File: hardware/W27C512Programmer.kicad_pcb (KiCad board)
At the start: 2 copper layers, 68.6 x 53.3 mm, 26 parts, among them Q1 Q_NPN_BCE, U1 AP3012, U2 LM339, U3 74HC595, U4 74HC595, U5 w27C512

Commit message: Getting ready for PCB..
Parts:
- added C10: 200uF, Capacitor_SMD:CP_Elec_6.3x5.4, F.Cu at (118.1, 36.8)
- added C11: 10uF, Capacitor_SMD:CP_Elec_5x5.4, F.Cu at (127.3, 54.6)
- added C7: 100nF, Capacitor_SMD:C_0603_1608Metric, F.Cu at (121.3, 90.2)
- added C8: 100nF, Capacitor_SMD:C_0603_1608Metric, F.Cu at (92.9, 55.6)
- added C9: 10uF, Capacitor_SMD:C_1206_3216Metric, F.Cu at (144.6, 57.1)
- added D10: 1N5819, Diode_SMD:D_SOD-123, F.Cu at (106.7, 55.2)
- added D11: 1N5819, Diode_SMD:D_SOD-123, F.Cu at (156.3, 71.8)
- added D12: 1N5819, Diode_SMD:D_SOD-123, F.Cu at (113.0, 55.2)
- added D2: GREEN, LED_SMD:LED_0603_1608Metric, F.Cu at (143.0, 95.2)
- added D3: GREEN, LED_SMD:LED_0603_1608Metric, F.Cu at (144.7, 95.2)
- added D4: GREEN, LED_SMD:LED_0603_1608Metric, F.Cu at (146.3, 95.2)
- added D5: GREEN, LED_SMD:LED_0603_1608Metric, F.Cu at (148.0, 95.2)
- added D6: GREEN, LED_SMD:LED_0603_1608Metric, F.Cu at (149.6, 95.2)
- added D7: GREEN, LED_SMD:LED_0603_1608Metric, F.Cu at (151.3, 95.2)
- added D8: GREEN, LED_SMD:LED_0603_1608Metric, F.Cu at (153.0, 95.2)
- added D9: RED, LED_SMD:LED_0603_1608Metric, F.Cu at (154.7, 95.2)
- added J1: CTRL, Connector_PinHeader_2.54mm:PinHeader_1x08_P2.54mm_Vertical, F.Cu at (134.6, 86.4)
- added J2: MSB, Connector_PinHeader_2.54mm:PinHeader_1x08_P2.54mm_Vertical, F.Cu at (114.3, 86.4)
- added J3: LSB, Connector_PinHeader_2.54mm:PinHeader_1x08_P2.54mm_Vertical, F.Cu at (94.0, 86.4)
- added J4: Ext_UART, Connector_PinHeader_2.54mm:PinHeader_1x03_P2.54mm_Vertical, F.Cu at (176.9, 52.1)
- added JP1: 24pin ROM VCC, Connector_PinHeader_2.54mm:PinHeader_1x03_P2.54mm_Vertical, F.Cu at (96.5, 56.5)
- added JP2: >=SST39SF020 needs A17, Connector_PinHeader_2.54mm:PinHeader_1x03_P2.54mm_Vertical, F.Cu at (96.6, 52.8)
- added Q2: 2N3906, Package_TO_SOT_SMD:SOT-23, F.Cu at (155.1, 54.1)
- added Q3: 2N3904, Package_TO_SOT_SMD:SOT-23, F.Cu at (155.0, 64.8)
- added Q4: 2N3904, Package_TO_SOT_SMD:SOT-23, F.Cu at (154.9, 84.0)
- added Q5: 2N3904, Package_TO_SOT_SMD:SOT-23, F.Cu at (153.0, 74.6)
- added Q6: 2N3906, Package_TO_SOT_SMD:SOT-23, F.Cu at (155.0, 61.2)
- added Q7: 2N3906, Package_TO_SOT_SMD:SOT-23, F.Cu at (154.9, 80.5)
- added Q8: 2N3906, Package_TO_SOT_SMD:SOT-23, F.Cu at (153.0, 71.0)
- added R12: 4k7, Resistor_SMD:R_0603_1608Metric, F.Cu at (144.7, 92.0)
- added R13: 4k7, Resistor_SMD:R_0603_1608Metric, F.Cu at (146.3, 92.0)
- added R14: 4k7, Resistor_SMD:R_0603_1608Metric, F.Cu at (148.0, 92.0)
- added R15: 4k7, Resistor_SMD:R_0603_1608Metric, F.Cu at (149.6, 92.0)
- added R16: 4k7, Resistor_SMD:R_0603_1608Metric, F.Cu at (151.3, 92.0)
- added R17: 4k7, Resistor_SMD:R_0603_1608Metric, F.Cu at (153.0, 92.0)
- added R18: 4k7, Resistor_SMD:R_0603_1608Metric, F.Cu at (154.7, 92.0)
- added R19: 22k, Resistor_SMD:R_0603_1608Metric, F.Cu at (108.9, 55.3)
- added R20: 22k, Resistor_SMD:R_0603_1608Metric, F.Cu at (106.9, 83.2)
- added R21: 22k, Resistor_SMD:R_0603_1608Metric, F.Cu at (110.5, 55.2)
- added R22: 1k, Resistor_SMD:R_0603_1608Metric, F.Cu at (172.7, 52.1)
- added R23: 22k, Resistor_SMD:R_0603_1608Metric, F.Cu at (152.2, 64.9)
- added R24: 22k, Resistor_SMD:R_0603_1608Metric, F.Cu at (151.5, 83.9)
- added R25: 22k, Resistor_SMD:R_0603_1608Metric, F.Cu at (149.3, 73.6)
- added R26: 4k7, Resistor_SMD:R_0603_1608Metric, F.Cu at (150.6, 61.3)
- added R27: 4k7, Resistor_SMD:R_0603_1608Metric, F.Cu at (149.8, 80.6)
- added R28: 4k7, Resistor_SMD:R_0603_1608Metric, F.Cu at (149.3, 71.9)
- added R29: 22k, Resistor_SMD:R_0603_1608Metric, F.Cu at (152.2, 61.3)
- added R30: 22k, Resistor_SMD:R_0603_1608Metric, F.Cu at (151.6, 80.5)
- added R31: 22k, Resistor_SMD:R_0603_1608Metric, F.Cu at (149.3, 70.2)
- added RV1: 50k, Potentiometer_SMD:Potentiometer_Bourns_TC33X_Vertical, F.Cu at (134.4, 56.5)
- C1: value 1uF -> 10uF; footprint Capacitor_SMD:C_0805_2012Metric -> Capacitor_SMD:C_1206_3216Metric
- C2, C4, C5, C6: footprint Capacitor_SMD:C_0805_2012Metric -> Capacitor_SMD:C_0603_1608Metric
- C3: value 1uF -> 100nF; footprint Capacitor_SMD:C_0805_2012Metric -> Capacitor_SMD:C_0603_1608Metric
- Q1: value Q_NPN_BCE -> 2N3904
- R1: value 9.8k -> 22k; footprint Resistor_SMD:R_0805_2012Metric -> Resistor_SMD:R_0603_1608Metric
- R10, R3, R6, R9: value 9.8k -> 4k7; footprint Resistor_SMD:R_0805_2012Metric -> Resistor_SMD:R_0603_1608Metric
- R11: value 470 -> 4k7; footprint Resistor_SMD:R_0805_2012Metric -> Resistor_SMD:R_0603_1608Metric
- R2: value 100k -> 22k; footprint Resistor_SMD:R_0805_2012Metric -> Resistor_SMD:R_0603_1608Metric
- R4: value 56k -> 22k; footprint Resistor_SMD:R_0805_2012Metric -> Resistor_SMD:R_0603_1608Metric
- R5: value 22k -> 270k; footprint Resistor_SMD:R_0805_2012Metric -> Resistor_SMD:R_0603_1608Metric
- R7: value 68k -> 4k7; footprint Resistor_SMD:R_0805_2012Metric -> Resistor_SMD:R_0603_1608Metric
- R8: value 1k5 -> 22k; footprint Resistor_SMD:R_0805_2012Metric -> Resistor_SMD:R_0603_1608Metric
- U1: value AP3012 -> MIC2288
- U2: value LM339 -> 74HC573; footprint Package_SO:SOIC-14_3.9x8.7mm_P1.27mm -> Package_SO:TSSOP-20_4.4x6.5mm_P0.65mm
- U3, U4: value 74HC595 -> 74HC573; footprint Package_SO:SOIC-16_3.9x9.9mm_P1.27mm -> Package_SO:TSSOP-20_4.4x6.5mm_P0.65mm
- U5: value w27C512 -> 28/32 pin ROM; footprint Socket:DIP_Socket-28_W11.9_W12.7_W15.24_W17.78_W18.5_3M_228-1277-00-0602J -> Socket:DIP_Socket-32_W11.9_W12.7_W15.24_W17.78_W18.5_3M_232-1285-00-0602J
- moved C3 61.4 mm to (91.1, 55.7), turned to 90 degrees
- moved C2 53.7 mm to (91.0, 52.4), turned to -90 degrees
- moved C6 47.8 mm to (97.2, 90.2), turned to -90 degrees
- moved U2 42.4 mm to (102.9, 92.7)
- moved R4 41.3 mm to (150.5, 54.1), turned to -90 degrees
- moved R5 39.7 mm to (150.5, 57.6), turned to -90 degrees
- moved R9 39.3 mm to (140.3, 55.9)
- moved R8 34.3 mm to (129.3, 59.7), turned to 180 degrees
- moved R6 33.0 mm to (140.3, 54.3)
- moved R7 31.6 mm to (140.3, 57.8)
- moved R10 29.9 mm to (140.3, 52.7), turned to 180 degrees
- moved R1 25.5 mm to (147.3, 53.3), turned to -90 degrees
- moved C1 21.0 mm to (144.6, 48.3), turned to 180 degrees
- moved D1 17.4 mm to (139.3, 48.3)
- moved L1 16.5 mm to (144.4, 50.8), turned to 180 degrees
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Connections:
- A1 pad 15: Net-(A1-Pad15) -> D0
- A1 pad 16: Net-(A1-Pad16) -> D1
- A1 pad 17: Net-(A1-Pad17) -> D2
- A1 pad 18: Net-(A1-Pad18) -> D3
- A1 pad 19: Net-(A1-Pad19) -> D4
- A1 pad 20: Net-(A1-Pad20) -> D5
- A1 pad 21: Net-(A1-Pad21) -> D6
- A1 pad 22: Net-(A1-Pad22) -> D7
- A1 pad 23: SRClock -> RLSBLE
- A1 pad 24: SRData -> RMSBLE
- A1 pad 25: ~{ROM_CE} -> ~{ROM_OE}
- A1 pad 26: VPE_ENABLE -> CTRL_LE
- A1 pad 27: ~{VPE_TO_VPP} -> unconnected-(A1-Pad27)
- A1 pad 28: unconnected-(A1-Pad28) -> ~{ROM_CE}
- A1 pad 9: ~{VPE_DISABLE} -> unconnected-(A1-Pad9)
- C3 pad 1: VPE -> +5V
- C6 pad 1: Net-(C6-Pad1) -> +5V
- Q1 pad 1: Net-(Q1-Pad1) -> GND
- Q1 pad 2: VPE -> Net-(Q1-Pad2)
- R1 pad 2: ~{VPE_DISABLE} -> ~{REG_DISABLE}
- R10 pad 1: VPE -> Net-(R10-Pad1)
- R10 pad 2: Net-(R10-Pad2) -> GND
- R11 pad 1: Net-(Q1-Pad3) -> Net-(D2-Pad1)
- R2 pad 1: VPE -> A16
- R2 pad 2: Net-(R2-Pad2) -> Net-(Q1-Pad2)
- R3 pad 1: Net-(R2-Pad2) -> Net-(Q1-Pad3)
- R3 pad 2: GND -> Net-(Q2-Pad2)
- R4 pad 1: +5V -> VPE
- R4 pad 2: Net-(C6-Pad1) -> Net-(Q2-Pad2)
- R5 pad 1: Net-(C6-Pad1) -> Net-(Q2-Pad3)
- R5 pad 2: GND -> Net-(R10-Pad1)
- R6 pad 1: VPE -> Net-(R6-Pad1)
- R6 pad 2: Net-(R6-Pad2) -> Net-(R10-Pad1)
- R7 pad 1: Net-(R6-Pad2) -> Net-(R6-Pad1)
- R7 pad 2: Net-(R7-Pad2) -> Net-(R10-Pad1)
- R8 pad 1: Net-(R8-Pad1) -> VPE
- R8 pad 2: Net-(R10-Pad2) -> Net-(R8-Pad2)
- R9 pad 1: Net-(Q1-Pad1) -> Net-(R6-Pad1)
- R9 pad 2: Net-(R6-Pad2) -> Net-(R10-Pad1)
- U1 pad 3: Net-(R2-Pad2) -> Net-(R10-Pad1)
- U1 pad 4: ~{VPE_DISABLE} -> ~{REG_DISABLE}
- U2 pad 1: Net-(R7-Pad2) -> GND
- U2 pad 10: Net-(C6-Pad1) -> GND
- U2 pad 11: VPE_ENABLE -> RLSBLE
- U2 pad 12: GND -> Net-(J3-Pad8)
- U2 pad 13: Net-(R10-Pad2) -> Net-(J3-Pad7)
- U2 pad 14: unconnected-(U2-Pad14) -> Net-(J3-Pad6)
- U2 pad 2: Net-(R6-Pad2) -> D0
- U2 pad 3: VPE -> D1
- U2 pad 4: Net-(C6-Pad1) -> D2
- U2 pad 5: VPE_ENABLE -> D3
- U2 pad 6: Net-(C6-Pad1) -> D4
- U2 pad 7: ~{VPE_TO_VPP} -> D5
- U2 pad 8: Net-(C6-Pad1) -> D6
- U2 pad 9: unconnected-(U2-Pad9) -> D7
- U3 pad 1: Net-(U3-Pad1) -> GND
- U3 pad 10: Net-(U3-Pad10) -> GND
- U3 pad 11: SRClock -> RMSBLE
- U3 pad 12: SRClock -> Net-(D11-Pad2)
- U3 pad 13: GND -> Net-(J2-Pad7)
- U3 pad 14: SRData -> Net-(J2-Pad6)
- U3 pad 15: Net-(U3-Pad15) -> Net-(J2-Pad5)
- U3 pad 16: +5V -> Net-(J2-Pad4)
- U3 pad 2: Net-(U3-Pad2) -> D0
- U3 pad 3: Net-(U3-Pad3) -> D1
- U3 pad 4: Net-(U3-Pad4) -> D2
- U3 pad 5: Net-(U3-Pad5) -> D3
- U3 pad 6: Net-(U3-Pad6) -> D4
- U3 pad 7: Net-(U3-Pad7) -> D5
- U3 pad 8: GND -> D6
- U3 pad 9: Net-(U3-Pad9) -> D7
- U4 pad 1: Net-(R8-Pad1) -> GND
- U4 pad 10: Net-(U3-Pad10) -> GND
- U4 pad 11: SRClock -> CTRL_LE
- U4 pad 12: SRClock -> ~{REG_DISABLE}
- U4 pad 13: GND -> ~{RW}
- U4 pad 14: Net-(U3-Pad9) -> A18
- U4 pad 15: Net-(U4-Pad15) -> A17
- U4 pad 16: +5V -> P1_VPP_ENABLE
- U4 pad 2: Net-(U4-Pad2) -> D0
- U4 pad 3: Net-(U4-Pad3) -> D1
- U4 pad 4: Net-(U4-Pad4) -> D2
- U4 pad 5: Net-(U4-Pad5) -> D3
- U4 pad 6: Net-(U4-Pad6) -> D4
- U4 pad 7: Net-(U4-Pad7) -> D5
- U4 pad 8: GND -> D6
- U4 pad 9: unconnected-(U4-Pad9) -> D7
- U5 pad 1: Net-(U4-Pad7) -> A18
- U5 pad 10: Net-(U3-Pad15) -> Net-(J3-Pad3)
- U5 pad 11: Net-(A1-Pad15) -> Net-(J3-Pad2)
- U5 pad 12: Net-(A1-Pad16) -> Net-(J3-Pad1)
- U5 pad 13: Net-(A1-Pad17) -> D0
- U5 pad 14: GND -> D1
- U5 pad 15: Net-(A1-Pad18) -> D2
- U5 pad 16: Net-(A1-Pad19) -> GND
- U5 pad 17: Net-(A1-Pad20) -> D3
- U5 pad 18: Net-(A1-Pad21) -> D4
- U5 pad 19: Net-(A1-Pad22) -> D5
- U5 pad 2: Net-(U4-Pad4) -> A16
- U5 pad 20: ~{ROM_CE} -> D6
- U5 pad 21: Net-(U4-Pad2) -> D7
- U5 pad 22: Net-(Q1-Pad3) -> ~{ROM_CE}
- U5 pad 23: Net-(U4-Pad3) -> Net-(J2-Pad3)
- U5 pad 24: Net-(R10-Pad2) -> Net-(D12-Pad1)
- U5 pad 25: Net-(U4-Pad15) -> Net-(J2-Pad4)
- U5 pad 26: Net-(U4-Pad5) -> Net-(D10-Pad1)
- U5 pad 27: Net-(U4-Pad6) -> Net-(J2-Pad1)
- U5 pad 28: +5V -> Net-(JP1-Pad2)
- U5 pad 3: Net-(U3-Pad7) -> Net-(D11-Pad1)
- U5 pad 4: Net-(U3-Pad6) -> Net-(J2-Pad5)
- U5 pad 5: Net-(U3-Pad5) -> Net-(J3-Pad8)
- U5 pad 6: Net-(U3-Pad4) -> Net-(J3-Pad7)
- U5 pad 7: Net-(U3-Pad3) -> Net-(J3-Pad6)
- U5 pad 8: Net-(U3-Pad2) -> Net-(J3-Pad5)
- U5 pad 9: Net-(U3-Pad1) -> Net-(J3-Pad4)
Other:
- board text added: "Reg. ON"

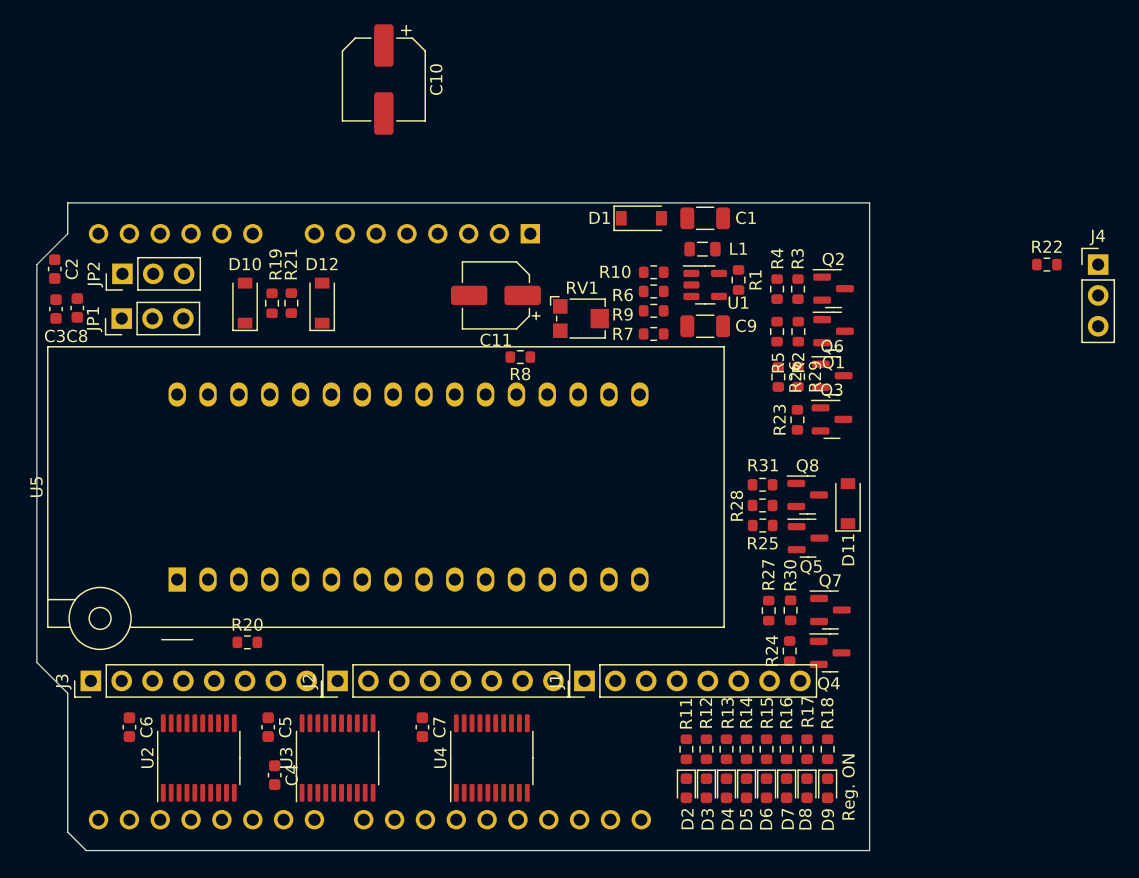
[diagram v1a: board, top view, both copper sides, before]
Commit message: PCB probably somewhat complete
Completely untested PCB. Maybe it works. Maybe I should look for someone to review...
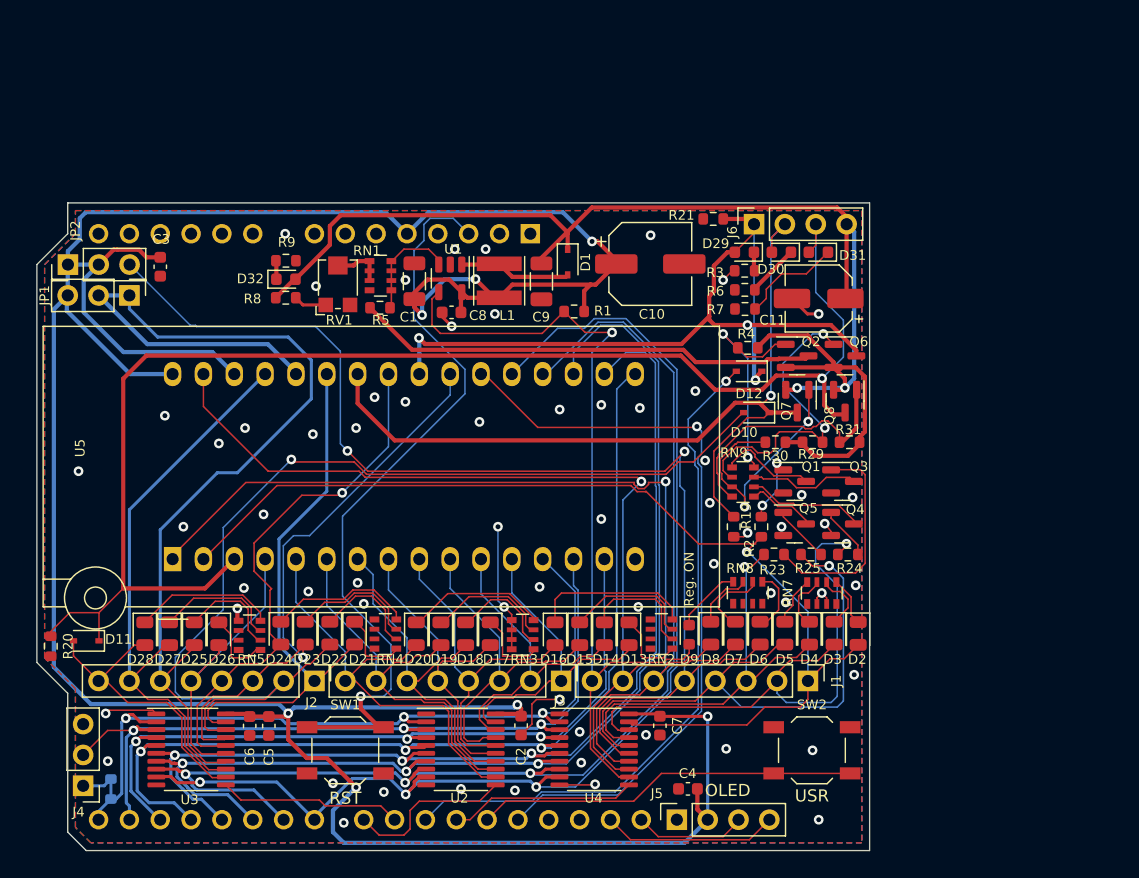
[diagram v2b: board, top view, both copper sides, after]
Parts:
- removed R10, R11, R12, R13, R14, R15, R16, R17, R18, R26, R27, R28: 4k7, Resistor_SMD:R_0603_1608Metric
- added D13: GREEN, LED_SMD:LED_0805_2012Metric, F.Cu at (138.3, 82.5)
- added D14: GREEN, LED_SMD:LED_0805_2012Metric, F.Cu at (136.3, 82.5)
- added D15: GREEN, LED_SMD:LED_0805_2012Metric, F.Cu at (134.2, 82.5)
- added D16: GREEN, LED_SMD:LED_0805_2012Metric, F.Cu at (132.2, 82.5)
- added D17: GREEN, LED_SMD:LED_0805_2012Metric, F.Cu at (126.9, 82.5)
- added D18: GREEN, LED_SMD:LED_0805_2012Metric, F.Cu at (124.8, 82.5)
- added D19: GREEN, LED_SMD:LED_0805_2012Metric, F.Cu at (122.8, 82.5)
- added D20: GREEN, LED_SMD:LED_0805_2012Metric, F.Cu at (120.8, 82.5)
- added D21: GREEN, LED_SMD:LED_0805_2012Metric, F.Cu at (115.7, 82.4)
- added D22: GREEN, LED_SMD:LED_0805_2012Metric, F.Cu at (113.7, 82.4)
- added D23: GREEN, LED_SMD:LED_0805_2012Metric, F.Cu at (111.6, 82.4)
- added D24: GREEN, LED_SMD:LED_0805_2012Metric, F.Cu at (109.6, 82.4)
- added D25: GREEN, LED_SMD:LED_0805_2012Metric, F.Cu at (104.5, 82.5)
- added D26: GREEN, LED_SMD:LED_0805_2012Metric, F.Cu at (102.5, 82.5)
- added D27: GREEN, LED_SMD:LED_0805_2012Metric, F.Cu at (100.5, 82.5)
- added D28: GREEN, LED_SMD:LED_0805_2012Metric, F.Cu at (98.4, 82.5)
- added D29: RED, LED_SMD:LED_0603_1608Metric, F.Cu at (147.8, 51.1)
- added D30: RED, LED_SMD:LED_0603_1608Metric, F.Cu at (150.9, 51.1)
- added D31: RED, LED_SMD:LED_0603_1608Metric, F.Cu at (153.9, 51.1)
- added D32: RED, LED_SMD:LED_0603_1608Metric, F.Cu at (110.0, 53.3)
- added J5: OLED, Connector_PinSocket_2.54mm:PinSocket_1x04_P2.54mm_Vertical, F.Cu at (142.2, 97.8)
- added J6: VP, Connector_PinSocket_2.54mm:PinSocket_1x04_P2.54mm_Vertical, F.Cu at (148.6, 48.7)
- added RN1: 4k7, Resistor_SMD:R_Array_Convex_4x0603, F.Cu at (117.8, 53.0)
- added RN2: 4k7, Resistor_SMD:R_Array_Convex_4x0603, F.Cu at (141.0, 82.5)
- added RN3: 4k7, Resistor_SMD:R_Array_Convex_4x0603, F.Cu at (129.5, 82.5)
- added RN4: 4k7, Resistor_SMD:R_Array_Convex_4x0603, F.Cu at (118.2, 82.5)
- added RN5: 4k7, Resistor_SMD:R_Array_Convex_4x0603, F.Cu at (107.0, 82.6)
- added RN7: 4k7, Resistor_SMD:R_Array_Convex_4x0603, F.Cu at (154.2, 79.1)
- added RN8: 4k7, Resistor_SMD:R_Array_Convex_4x0603, F.Cu at (148.1, 79.1)
- added RN9: 4k7, Resistor_SMD:R_Array_Convex_4x0603, F.Cu at (147.7, 70.0)
- added SW1: RST, Button_Switch_SMD:SW_SPST_TL3342, F.Cu at (114.9, 92.1)
- added SW2: USR, Button_Switch_SMD:SW_SPST_TL3342, F.Cu at (153.4, 92.1)
- C10: value 200uF -> 220uF
- C11: value 10uF -> NC
- D1, D10, D11, D12: footprint Diode_SMD:D_SOD-123 -> Diode_SMD:D_SOD-323
- D2, D3, D4, D5, D6, D7, D8: footprint LED_SMD:LED_0603_1608Metric -> LED_SMD:LED_0805_2012Metric
- L1: footprint Inductor_SMD:L_0805_2012Metric -> Inductor_SMD:L_Taiyo-Yuden_MD-4040
- Q1, Q3, Q4, Q5: value 2N3904 -> MMBT3904
- Q2, Q6, Q7, Q8: value 2N3906 -> MMBT3906
- R22: value 1k -> NC; moved to B.Cu
- R3, R6, R7, R9: value 4k7 -> 22k
- moved J4 94.0 mm to (93.3, 95.0), turned to 180 degrees
- moved R22 88.4 mm to (95.6, 95.3), turned to 90 degrees
- moved D11 63.7 mm to (93.6, 83.1), turned to 180 degrees
- moved C2 53.7 mm to (129.4, 90.0)
- moved D10 43.1 mm to (148.8, 64.3), turned to 180 degrees
- moved R19 42.2 mm to (146.9, 73.7), turned to -90 degrees
- moved J3 38.7 mm to (132.7, 86.4), turned to -90 degrees
- moved D12 35.6 mm to (148.2, 60.9), turned to 180 degrees
- moved R21 35.4 mm to (145.2, 48.3), turned to 180 degrees
- moved C4 34.1 mm to (143.2, 95.2), turned to 180 degrees
- moved R5 32.8 mm to (117.8, 55.6), turned to 0 degrees
- moved C8 30.8 mm to (123.7, 56.0), turned to 180 degrees
- moved R9 30.6 mm to (110.0, 51.8)
- moved C10 26.7 mm to (140.1, 52.0), turned to 0 degrees
- moved C11 26.6 mm to (153.9, 54.9)
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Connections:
- net Net-(D10-Pad2) renamed /A9
- net Net-(D11-Pad2) renamed /A15
- net Net-(J2-Pad1) renamed /A8
- net Net-(J2-Pad3) renamed /A10
- net Net-(J2-Pad4) renamed /A11
- net Net-(J2-Pad5) renamed /A12
- net Net-(J2-Pad7) renamed /A14
- net Net-(J3-Pad1) renamed /A0
- net Net-(J3-Pad2) renamed /A1
- net Net-(J3-Pad3) renamed /A2
- net Net-(J3-Pad4) renamed /A3
- net Net-(J3-Pad5) renamed /A4
- net Net-(J3-Pad6) renamed /A5
- net Net-(J3-Pad7) renamed /A6
- net Net-(J3-Pad8) renamed /A7
- A1 pad 13: unconnected-(A1-Pad13) -> SDA2
- A1 pad 14: unconnected-(A1-Pad14) -> SCL2
- A1 pad 27: unconnected-(A1-Pad27) -> Net-(A1-Pad27)
- A1 pad 3: unconnected-(A1-Pad3) -> Net-(A1-Pad3)
- A1 pad 31: unconnected-(A1-Pad31) -> SDA
- A1 pad 32: unconnected-(A1-Pad32) -> SCL
- J2 pad 6: Net-(J2-Pad6) -> /A13
- J4 pad 1: Net-(J4-Pad1) -> D0
- JP1 pad 1: Net-(J2-Pad6) -> /A13
- JP1 pad 2: Net-(JP1-Pad2) -> /A13
- JP2 pad 2: Net-(JP2-Pad2) -> +5V
- Q1 pad 1: GND -> Net-(Q1-Pad1)
- Q1 pad 2: Net-(Q1-Pad2) -> GND
- Q2 pad 1: VPE -> Net-(Q2-Pad1)
- Q2 pad 2: Net-(Q2-Pad2) -> VPE
- Q3 pad 1: GND -> Net-(Q3-Pad1)
- Q3 pad 2: Net-(Q3-Pad2) -> GND
- Q4 pad 1: GND -> Net-(Q4-Pad1)
- Q4 pad 2: Net-(Q4-Pad2) -> GND
- Q5 pad 1: GND -> Net-(Q5-Pad1)
- Q5 pad 2: Net-(Q5-Pad2) -> GND
- Q6 pad 1: VPE -> Net-(Q6-Pad1)
- Q6 pad 2: Net-(Q6-Pad2) -> VPE
- Q7 pad 1: VPE -> Net-(Q7-Pad1)
- Q7 pad 2: Net-(Q7-Pad2) -> VPE
- Q8 pad 1: VPE -> Net-(Q8-Pad1)
- Q8 pad 2: Net-(Q8-Pad2) -> VPE
- R2 pad 2: Net-(Q1-Pad2) -> Net-(Q1-Pad1)
- R22 pad 1: Net-(J4-Pad1) -> D0
- R23 pad 2: Net-(Q3-Pad2) -> Net-(Q3-Pad1)
- R24 pad 2: Net-(Q4-Pad2) -> Net-(Q4-Pad1)
- R25 pad 2: Net-(Q5-Pad2) -> Net-(Q5-Pad1)
- R29 pad 2: Net-(Q6-Pad2) -> Net-(Q6-Pad1)
- R3 pad 1: Net-(Q1-Pad3) -> Net-(D29-Pad1)
- R3 pad 2: Net-(Q2-Pad2) -> GND
- R30 pad 2: Net-(Q7-Pad2) -> Net-(Q7-Pad1)
- R31 pad 2: Net-(Q8-Pad2) -> Net-(Q8-Pad1)
- R4 pad 2: Net-(Q2-Pad2) -> Net-(Q2-Pad1)
- R5 pad 2: Net-(R10-Pad1) -> Net-(RN1-Pad5)
- R6 pad 1: Net-(R6-Pad1) -> Net-(D30-Pad1)
- R6 pad 2: Net-(R10-Pad1) -> GND
- R7 pad 1: Net-(R6-Pad1) -> Net-(D31-Pad1)
- R7 pad 2: Net-(R10-Pad1) -> GND
- R9 pad 1: Net-(R6-Pad1) -> Net-(D32-Pad1)
- R9 pad 2: Net-(R10-Pad1) -> GND
- RV1 pad 2: Net-(R6-Pad1) -> Net-(RN1-Pad1)
- U1 pad 3: Net-(R10-Pad1) -> Net-(RN1-Pad5)
- U3 pad 14: Net-(J2-Pad6) -> /A13
- U5 pad 28: Net-(JP1-Pad2) -> /A13
- U5 pad 30: Net-(JP2-Pad2) -> +5V
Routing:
- net +5V: track 0.00 -> 269.7 mm, vias 0 -> 7
- net Net-(D11-Pad1): track 0.00 -> 118.9 mm, vias 0 -> 1
- net VPE: track 0.00 -> 112.7 mm, vias 0 -> 2
- net D6: track 0.00 -> 100.4 mm, vias 0 -> 3
- net D7: track 0.00 -> 97.7 mm, vias 0 -> 3
- net A17: track 0.00 -> 97.6 mm, vias 0 -> 2
- net D5: track 0.00 -> 94.5 mm, vias 0 -> 3
- net D4: track 0.00 -> 87.6 mm, vias 0 -> 3
- net /A9: track 0.00 -> 87.5 mm, vias 0 -> 1
- net A16: track 0.00 -> 87.1 mm, vias 0 -> 1
- net /A13: track 0.00 -> 85.6 mm
- net D3: track 0.00 -> 81.8 mm, vias 0 -> 3
- net A18: track 0.00 -> 80.3 mm, vias 0 -> 1
- net ~{RW}: track 0.00 -> 76.9 mm, vias 0 -> 1
- net Net-(D10-Pad1): track 0.00 -> 72.0 mm, vias 0 -> 1
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- added copper zone on B.Cu, net GND
- added copper zone on F.Cu, net GND
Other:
- board text added: "Relatively Universal ROM Programmer rev 0 ABNielsen.com/65uino"

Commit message: Hardware release day update!
Gerber files (zip) BOM, placement and KiCAD files as they are for Rev0
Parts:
- removed R22: NC, Resistor_SMD:R_0603_1608Metric
- added D33: 1N5819, Diode_SMD:D_SOD-323, F.Cu at (94.6, 81.5)
- added J7: SAO, Connector_PinHeader_2.54mm:PinHeader_2x03_P2.54mm_Vertical, B.Cu at (102.2, 52.1)
- added JP3: W27C010/AT27C010 needs p1 VPE/VPP (32 pin), Jumper:SolderJumper-3_P1.3mm_Open_RoundedPad1.0x1.5mm, B.Cu at (94.6, 57.3)
- added R10: 1k, Resistor_SMD:R_0603_1608Metric, F.Cu at (96.6, 95.3)
- added R11: 1k, Resistor_SMD:R_0603_1608Metric, F.Cu at (96.6, 92.2)
- added R12: 22k, Resistor_SMD:R_0603_1608Metric, F.Cu at (90.5, 83.4)
- JP1: footprint Connector_PinHeader_2.54mm:PinHeader_1x03_P2.54mm_Vertical -> Connector_PinHeader_2.54mm:PinHeader_1x03_P2.54mm_Vertical_SolderJumpers
- JP2: value >=SST39SF020 needs A17 -> >=SST39SF020 & 28C512 need A17; footprint Connector_PinHeader_2.54mm:PinHeader_1x03_P2.54mm_Vertical -> Connector_PinHeader_2.54mm:PinHeader_1x03_P2.54mm_Vertical_SolderJumpers
- moved R20 1.38 mm to (92.0, 83.4)
- moved D11 1.09 mm to (94.6, 83.5)
- moved R8 0.93 mm to (111.0, 54.8)
- moved D32 0.93 mm to (111.0, 53.3)
- moved R9 0.93 mm to (111.0, 51.8)
- moved RN1 0.08 mm to (117.9, 53.0)
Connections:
- A1 pad 10: unconnected-(A1-Pad10) -> Net-(A1-Pad10)
- A1 pad 4: unconnected-(A1-Pad4) -> Net-(A1-Pad4)
- A1 pad 9: unconnected-(A1-Pad9) -> Net-(A1-Pad9)
- D31 pad 2: Net-(D11-Pad1) -> Net-(D31-Pad2)
- J4 pad 1: D0 -> Net-(J4-Pad1)
- J4 pad 2: D1 -> Net-(J4-Pad2)
- J6 pad 3: Net-(D11-Pad1) -> Net-(D31-Pad2)
- JP1 pad 2: /A13 -> Net-(JP1-Pad2)
- JP2 pad 2: +5V -> Net-(JP2-Pad2)
- Q8 pad 3: Net-(D11-Pad1) -> Net-(D31-Pad2)
- R5 pad 2: Net-(RN1-Pad5) -> Net-(R5-Pad2)
- RN1 pad 3: Net-(RN1-Pad1) -> Net-(R5-Pad2)
- RN1 pad 4: GND -> Net-(R5-Pad2)
- RN1 pad 5: Net-(RN1-Pad5) -> GND
- RN1 pad 6: Net-(RN1-Pad5) -> Net-(RN1-Pad6)
- RN1 pad 7: Net-(RN1-Pad5) -> Net-(RN1-Pad6)
- RN1 pad 8: Net-(RN1-Pad5) -> Net-(RN1-Pad6)
- U1 pad 3: Net-(RN1-Pad5) -> Net-(R5-Pad2)
- U5 pad 1: A18 -> Net-(U5-Pad1)
- U5 pad 28: /A13 -> Net-(JP1-Pad2)
- U5 pad 30: +5V -> Net-(JP2-Pad2)
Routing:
- net Net-(D31-Pad2): track 0.00 -> 84.6 mm, vias 0 -> 2
- net Net-(D11-Pad1): track 118.9 -> 48.0 mm, vias 1 -> 3
- net Net-(U5-Pad1): track 0.00 -> 36.6 mm, vias 0 -> 2
- net +5V: track 269.7 -> 239.7 mm, vias 7 -> 5
- net Net-(JP2-Pad2): track 0.00 -> 28.6 mm, vias 0 -> 1
- net Net-(A1-Pad4): track 0.00 -> 21.4 mm
- net /A13: track 85.6 -> 64.6 mm
- net Net-(JP1-Pad2): track 0.00 -> 19.7 mm
- net SCL2: track 0.00 -> 11.5 mm
- net Net-(R5-Pad2): track 0.00 -> 10.9 mm
- net SDA2: track 0.00 -> 9.66 mm
- net A18: track 80.3 -> 89.7 mm
- net Net-(RN1-Pad5): track 8.34 -> 0.00 mm
- net Net-(A1-Pad10): track 0.00 -> 6.13 mm
- net GND: track 34.2 -> 39.5 mm, vias 63 -> 75
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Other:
- board text added: "24 pins"
- board text added: "28 Pins"
- board text added: "32 Pins"
- board text added: "3v3"
- board text added: "5V"
- board text added: "A"
- board text added: "A0"
- board text added: "A1"
- board text added: "A13"
- board text added: "A15"
- board text added: "A17"
- board text added: "A18"
- board text added: "A8"
- board text added: "A9 VPE Enable"
- board text added: "A9 VPP"
- board text added: "B"
- board text added: "C"
- board text added: "D"
- board text added: "GND"
- board text added: "P1 VPP"
- board text added: "Pin1->"
- board text added: "Pins Short on JP1/JP2/JP3 24pin B to 5V 28pin A to 5V, B to A13 32pin B to A13, A to A17* VPP alt Pin1 VPP to C* or D* * = If needed"
- board text added: "RX"
- board text added: "SCL"
- board text added: "SDA"
- board text added: "TX"
- board text added: "VPE"
- board text added: "VPE Enable"
- board text added: "VPE_TO_VPP / A16"
- board text added: "VPP"
- board text added: "VPP (OE)"
- board text added: "{dblquote}Pin 1{dblquote} VPE Enable"
- board text added: "~{RW}"
- board text added: "~{Reg. Off}"
- board text removed: "Reg. ON"
